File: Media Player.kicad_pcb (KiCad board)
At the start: 4 copper layers, 114.3 x 68.5 mm, 144 parts, among them J1 12402012E212A, J10 MEM2075-00-140-01-A, J40 PH2.0, J41 UART, J70 SJ-3524-SMT-TR, Q10 DMP3068L-7, Q40 DMP3068L-7, Q50 DMP3068L-7, Q70 DMP3068L-7, SW30 BOOT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

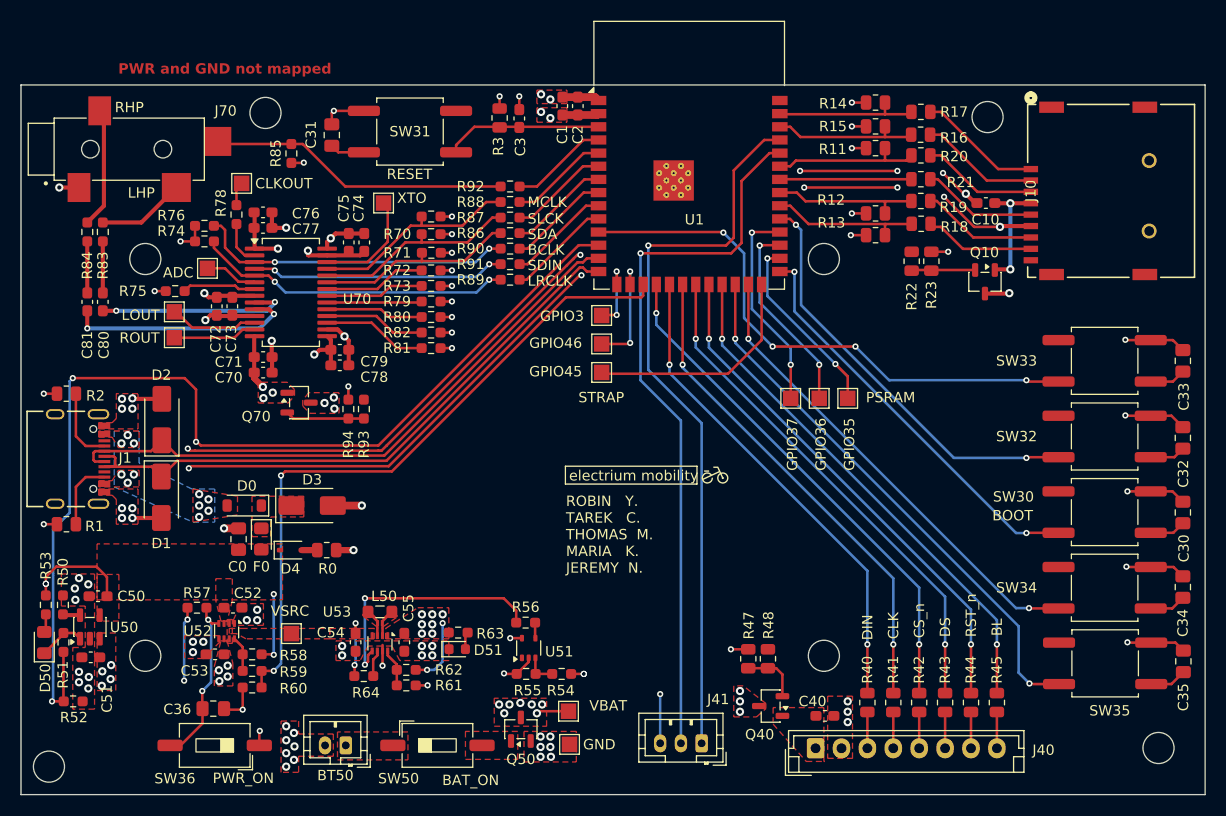
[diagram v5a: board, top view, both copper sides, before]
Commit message: Most DRC errors removed EXCEPT USB
USB receptacle pins are too close to each  other and the design rules I set are upset

(31 errors, 1.9mm instead of the minimum 2.0mm)
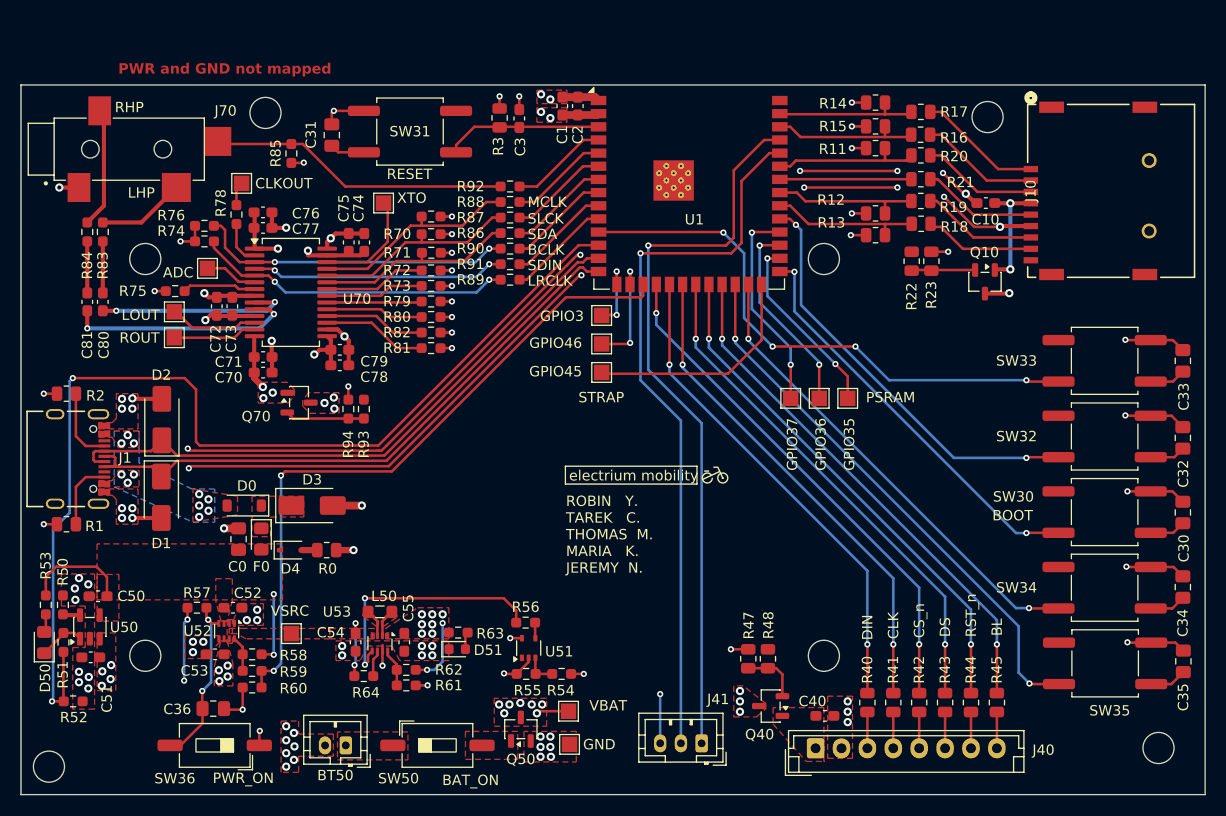
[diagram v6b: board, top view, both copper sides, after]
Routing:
- net Net-(U1-IO35): track 19.6 -> 17.9 mm
- net VBUS: vias 4 -> 2
- net VBAT: vias 19 -> 18
- net /CHRG_STAT: vias 3 -> 2
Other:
- board text added: "U70"
- board text removed: "${REFERENCE}"
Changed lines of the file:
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@@
 		(attr smd)
 		(fp_line
-			(start -9.2 -12.9)
-			(end -9.2 -6.7)
-			(stroke
-				(width 0.12)
-				(type solid)
-			)
-			(layer "F.SilkS")
-		)
-		(fp_line
-			(start -9.2 -12.9)
-			(end 9.2 -12.9)
-			(stroke
-				(width 0.12)
-				(type solid)
-			)
-			(layer "F.SilkS")
-		)
-		(fp_line
 			(start -9.2 11.95)
 			(end -9.2 12.95)
@@
 		)
 		(fp_line
-			(start 9.2 -12.9)
-			(end 9.2 -6.7)
-			(stroke
-				(width 0.12)
-				(type solid)
-			)
-			(layer "F.SilkS")
-		)
-		(fp_line
 			(start 9.2 12.95)
 			(end 7.7 12.95)
@@
 		)
 	)
-	(gr_text "${REFERENCE}"
+	(gr_text "U70"
 		(at 112.25 60.025 0)
 		(layer "F.Fab")
@@
 	)
 	(via
-		(at 140.525 96.85)
-		(size 0.6)
-		(drill 0.3)
-		(layers "F.Cu" "B.Cu")
-		(net 3)
-	)
-	(via
 		(at 102.275 91.6)
 		(size 0.6)
@@
 	)
 	(via
-		(at 88.6 88.15)
-		(size 0.6)
-		(drill 0.3)
-		(layers "F.Cu" "B.Cu")
-		(net 4)
-	)
-	(via
-		(at 88.6 88.15)
-		(size 0.6)
-		(drill 0.3)
-		(layers "F.Cu" "B.Cu")
-		(net 4)
-	)
-	(via
 		(at 110.6 89.15)
 		(size 0.6)
@@
 	)
 	(segment
-		(start 102 68.3)
-		(end 103.1 69.4)
+		(start 140.03 55.47)
+		(end 120.7 74.8)
 		(width 0.25)
 		(layer "F.Cu")
@@
 	)
 	(segment
-		(start 90.3 94.725)
-		(end 90.3 99.475)
+		(start 120.7 74.8)
+		(end 103.45 74.8)
 		(width 0.25)
 		(layer "F.Cu")
@@
 	)
 	(segment
-		(start 103.55 74.8)
-		(end 120.7 74.8)
+		(start 90.3 94.725)
+		(end 90.3 99.475)
 		(width 0.25)
 		(layer "F.Cu")
@@
 	)
 	(segment
-		(start 90.325 99.5)
-		(end 89.2 99.5)
+		(start 103.45 74.8)
+		(end 103.1 74.45)
 		(width 0.25)
 		(layer "F.Cu")
@@
 	)
 	(segment
-		(start 103.2 74.45)
-		(end 103.55 74.8)
+		(start 102 68.3)
+		(end 91.2 68.3)
 		(width 0.25)
 		(layer "F.Cu")
@@
 	)
 	(segment
-		(start 91.2 68.3)
-		(end 102 68.3)
+		(start 90.325 99.5)
+		(end 89.2 99.5)
 		(width 0.25)
 		(layer "F.Cu")
@@
 	(segment
 		(start 103.1 69.4)
-		(end 103.1 74.45)
-		(width 0.25)
-		(layer "F.Cu")
-		(net 55)
-	)
-	(segment
-		(start 140.03 55.47)
-		(end 141.95 55.47)
+		(end 102 68.3)
 		(width 0.25)
 		(layer "F.Cu")
@@
 	)
 	(segment
-		(start 103.1 74.45)
-		(end 103.2 74.45)
+		(start 141.95 55.47)
+		(end 140.03 55.47)
 		(width 0.25)
 		(layer "F.Cu")
@@
 	)
 	(segment
-		(start 120.7 74.8)
-		(end 140.03 55.47)
+		(start 103.1 74.45)
+		(end 103.1 69.4)
 		(width 0.25)
 		(layer "F.Cu")
@@
 	)
 	(via
-		(at 103.1 74.45)
-		(size 0.6)
-		(drill 0.3)
-		(layers "F.Cu" "B.Cu")
-		(net 55)
-	)
-	(via
 		(at 91.2 68.3)
 		(size 0.6)
@@
 	)
 	(segment
-		(start 166 68.125)
+		(start 164.8125 66.9375)
 		(end 158.25 60.375)
 		(width 0.25)
@@
 		(polygon
 			(pts
-				(xy 93.5 108) (xy 141.4 108) (xy 141.4 95.5) (xy 108 95.5) (xy 108 95.5) (xy 93.5 95.5)
+				(xy 93.5 108) (xy 141.4 108) (xy 141.4 95.5) (xy 108 95.5) (xy 93.5 95.5)
 			)
 		)

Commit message: Copper Ground Pour, Traces Moved to Upper Layer
Replaced gnd trace around D+ D- and SDIO CLK with full board GND pour. DRC issues with gnd pour right now. Also moved a lot of un-necessary back layer signal traces to top layer. DRC still somewhat unfixed.
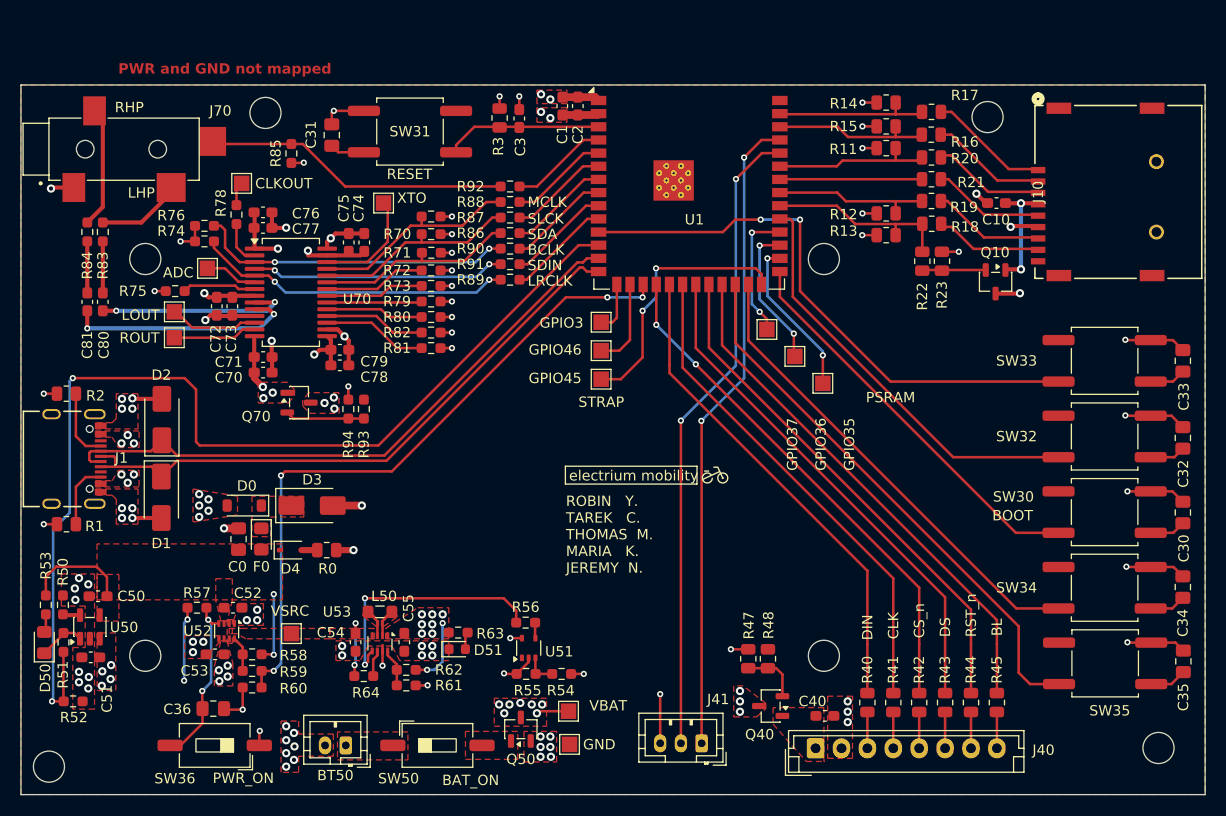
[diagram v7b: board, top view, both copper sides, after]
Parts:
- moved TP5 7.04 mm to (158.2, 63.6)
- moved TP4 4.68 mm to (160.9, 66.2)
- moved TP3 2.80 mm to (163.6, 68.8)
- moved R20 1.04 mm to (174.1, 47.0)
- moved C10 1.03 mm to (180.4, 51.4)
- moved Q10 1.03 mm to (180.3, 59.0)
- moved R11 1.03 mm to (169.7, 46.1)
- moved R12 1.03 mm to (169.7, 52.4)
- moved R13 1.03 mm to (169.7, 54.5)
- moved R14 1.03 mm to (169.7, 41.7)
- moved R15 1.03 mm to (169.7, 44.0)
- moved R16 1.03 mm to (174.1, 44.8)
- moved R17 1.03 mm to (174.1, 42.6)
- moved R18 1.03 mm to (174.1, 53.4)
- moved R19 1.03 mm to (174.1, 51.2)
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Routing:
- net GND: track 228.0 -> 109.7 mm, vias 91 -> 81
- net /TXD0: track 70.9 -> 62.3 mm, vias 1 -> 2
- net /RXD0: track 69.7 -> 61.9 mm, vias 1 -> 2
- net Net-(U1-IO37): track 20.3 -> 12.7 mm
- net Net-(U1-IO36): track 19.1 -> 14.1 mm
- net /SD_D1: track 14.5 -> 18.3 mm
- net Net-(U1-IO45): track 22.3 -> 25.4 mm, vias 0 -> 2
- net Net-(U1-IO35): track 17.9 -> 15.5 mm
- net Net-(U1-IO46): track 11.0 -> 8.57 mm, vias 2 -> 0
- net Net-(U1-IO3): track 7.07 -> 4.91 mm, vias 2 -> 0
- net /PB1: track 57.5 -> 58.9 mm, vias 4 -> 2
- net /PB2: track 50.9 -> 49.6 mm, vias 2 -> 0
- net /SD_D3: track 14.2 -> 15.2 mm
- net /SD_D2: track 13.8 -> 14.9 mm
- net /SD_D0: track 14.2 -> 15.3 mm
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- added copper zone on In2.Cu, net /USB_PWR
- removed copper zone on B.Cu, net /USB_PWR
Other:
- board text added: "Change gnd traces on USB and SDIO to copper pour (need stitching?)"
- board text added: "Check out copper pour priority override"
- board text added: "Perchance use larger inductor to reduce overheating? Also for costs"
- board text added: "Reconsider rerouting this trace for CHRGSTAT"
- board text added: "Use calculator for trace widths for power"

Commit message: Minor Changes
Power traces enlarged, certain pad and hole clearances on USB modified, still within design rules, fixed silk screen clearance, copper pours now with thermal relief for pads connected to large planes. Most DRC's resolved. Design rule constraints tuned very slightly.
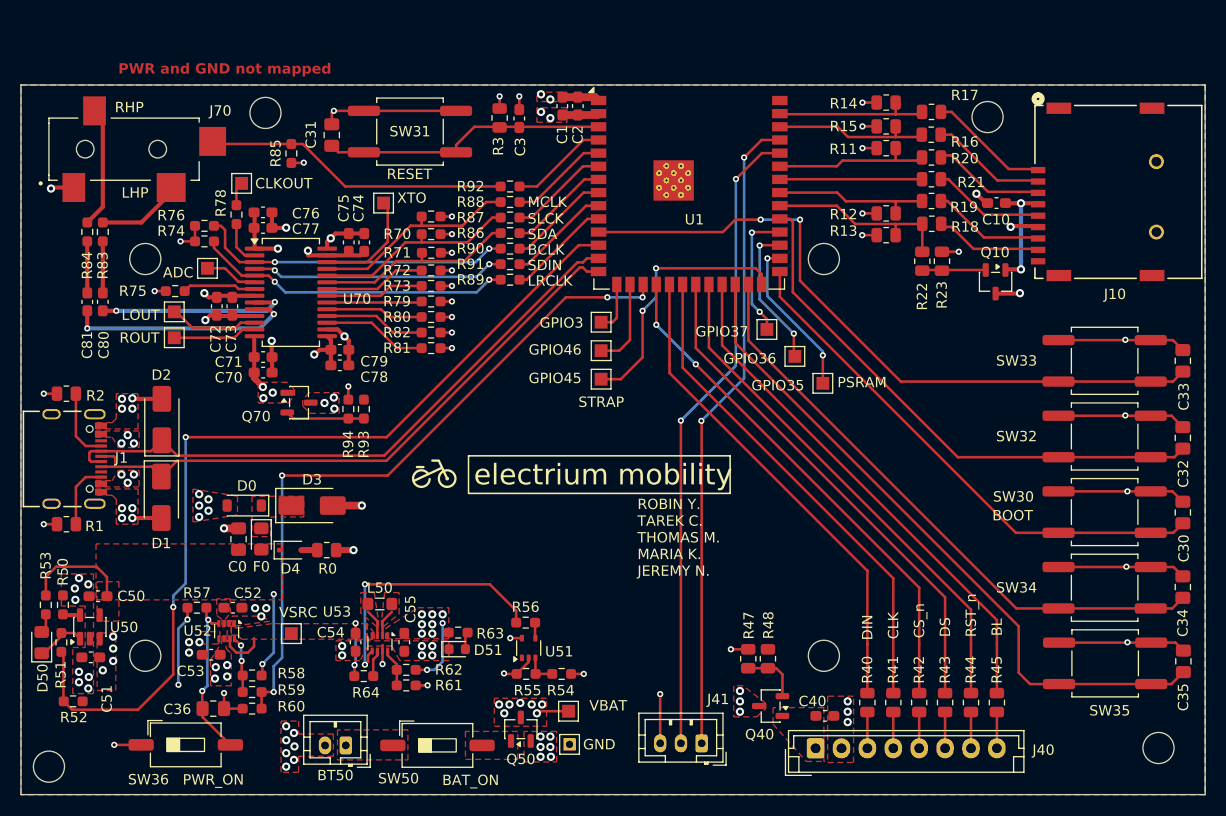
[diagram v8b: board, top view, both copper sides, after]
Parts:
- F0: value 0805L050WR -> 0805L075WR
- TP14, TP3, TP4, TP5, TP50, TP52, TP6, TP7, TP70, TP71, TP72, TP73, TP8: footprint TestPoint:TestPoint_Pad_1.5x1.5mm -> footprints:TestPoint_Pad_1.5x1.5mm
- TP51: footprint TestPoint:TestPoint_Pad_1.5x1.5mm -> TestPoint:TestPoint_THTPad_1.5x1.5mm_Drill0.7mm
- moved G*** 27.1 mm to (126.1, 77.6)
- moved SW36 2.80 mm to (102.1, 103.7), turned to 0 degrees
- moved R58 2.04 mm to (108.5, 97.0)
- moved R60 2.04 mm to (108.5, 100.2)
- moved R59 2.04 mm to (108.5, 98.6)
- moved L50 0.76 mm to (120.8, 90.1)
- moved C53 0.38 mm to (104.6, 95.0)
- moved D50 0.25 mm to (88.2, 93.8)
- moved R51 0.20 mm to (90.1, 93.8)
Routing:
- net GND: track 109.7 -> 151.9 mm
- net /CHRG_STAT: track 102.3 -> 88.0 mm
- net /PB2: track 49.6 -> 58.5 mm
- net /GPIO0: track 42.3 -> 51.2 mm
- net /PB3: track 56.7 -> 65.6 mm
- net /CHIP_PU: track 18.5 -> 27.4 mm
- net /PB0: track 44.1 -> 52.8 mm
- net /PB1: track 58.9 -> 67.2 mm
- net VSRC: track 6.13 -> 10.5 mm
- net /PWR_SRC: track 65.2 -> 67.3 mm
- net Net-(U52-ST): track 3.43 -> 5.47 mm, vias 0 -> 2
- net /Power/BB_EN: track 24.3 -> 26.2 mm
- net VBUS: track 17.8 -> 19.1 mm
- net VBAT: track 11.5 -> 12.2 mm
- added copper zone on B.Cu, net GND
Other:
- board text added: "Changed pad clearance for USB because manufacturer footprint is designed wrong."
- board text added: "Check with Damir the thickness of dielectric and copper"
- board text added: "Double check that your that your parts are IN STOCK"
- board text added: "Use calculator for trace widths for power Might need to change design constraints for better power routing"
- board text added: "move pwr_src down and connect vsrc from outside the IC too, use via to connect to pwr_src"
- board text added: "widen vsrc trace or shorten"
- board text removed: "How many vias do I actually need for power to plane ?"
- board text removed: "Perchance use larger inductor to reduce overheating? Also for costs"
- board text removed: "Power pours/traces are small? Especially VSRC"
- board text removed: "Reconsider rerouting this trace for CHRGSTAT"
- board text removed: "Use calculator for trace widths for power"
